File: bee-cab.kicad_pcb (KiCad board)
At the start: 2 copper layers, 29 x 53.3 mm, 34 parts, among them J1 Conn_01x02_Male, J10 Conn_01x01, J11 Conn_02x01, J12 Conn_02x01, J13 Conn_01x02, J14 Conn_01x02, J15 Conn_01x02, J16 Conn_01x02, J17 Conn_01x03, J18 Conn_01x02, J19 Conn_01x02, J2 Conn_01x02_Male, J3 Conn_01x02_Male, J4 Conn_01x02_Male, J5 Conn_01x03, J6 Conn_02x03_Odd_Even, J7 Conn_02x01, J8 Conn_01x02, J9 Conn_01x02

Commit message: Layout.
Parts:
- moved J7 2.54 mm to (85.1, 118.1), turned to 270 degrees
- moved R2 1.27 mm to (88.9, 130.8)
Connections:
- C2 pad 2: Net-(C1-Pad2) -> Net-(C1-Pad1)
- J17 pad 1: Net-(C1-Pad2) -> Net-(C1-Pad1)
- J18 pad 1: Net-(C1-Pad2) -> Net-(C1-Pad1)
- J18 pad 2: Net-(C1-Pad2) -> Net-(C1-Pad1)
- J5 pad 3: Net-(C1-Pad2) -> Net-(C1-Pad1)
- J6 pad 1: Net-(C1-Pad1) -> Net-(C1-Pad2)
- J7 pad 1: Net-(C1-Pad2) -> Net-(C1-Pad1)
- J9 pad 1: Net-(C1-Pad2) -> Net-(C1-Pad1)
- J9 pad 2: Net-(C1-Pad2) -> Net-(C1-Pad1)
- R1 pad 2: Net-(C1-Pad2) -> Net-(C1-Pad1)
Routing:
- net -15V: track 0.00 -> 97.9 mm, vias 1 -> 0
- net Net-(C1-Pad1): track 0.00 -> 76.7 mm
- net +15V: track 0.00 -> 61.8 mm
- net GND: track 0.00 -> 47.3 mm
- net Net-(J12-Pad1): track 0.00 -> 21.6 mm
- net +5V: track 0.00 -> 21.3 mm
- net Net-(C1-Pad2): track 0.00 -> 15.0 mm
- net Net-(R2-Pad1): track 0.00 -> 6.77 mm, vias 1 -> 0
- net Net-(J7-Pad2): track 0.00 -> 5.08 mm
- net Net-(J12-Pad2): track 0.00 -> 4.05 mm
- net Net-(J11-Pad2): track 0.00 -> 4.05 mm
- net Net-(J6-Pad5): track 0.00 -> 3.81 mm
- net Net-(C2-Pad1): track 0.00 -> 3.81 mm
- net (no net): vias 2 -> 4
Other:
- net class Default: trace_width 0.25 -> 0.5

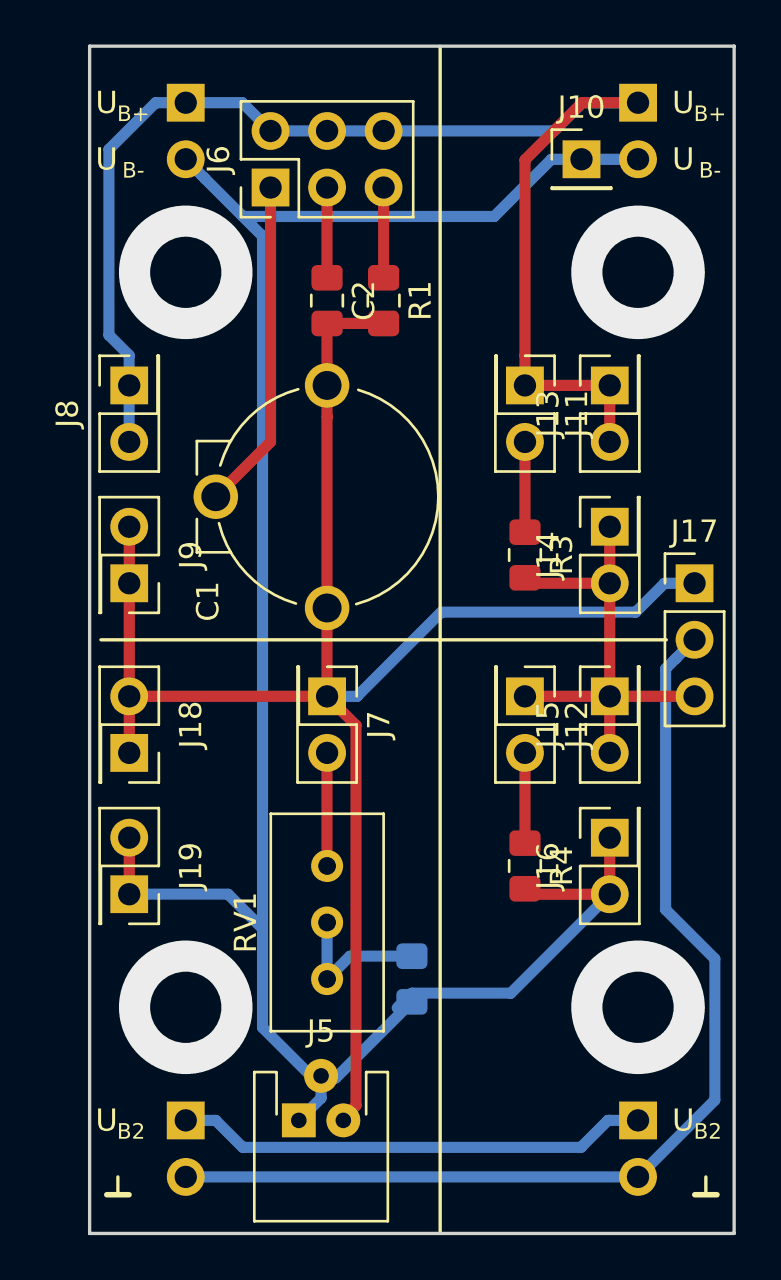
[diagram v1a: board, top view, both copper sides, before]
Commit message: Place part references on silkscreen.
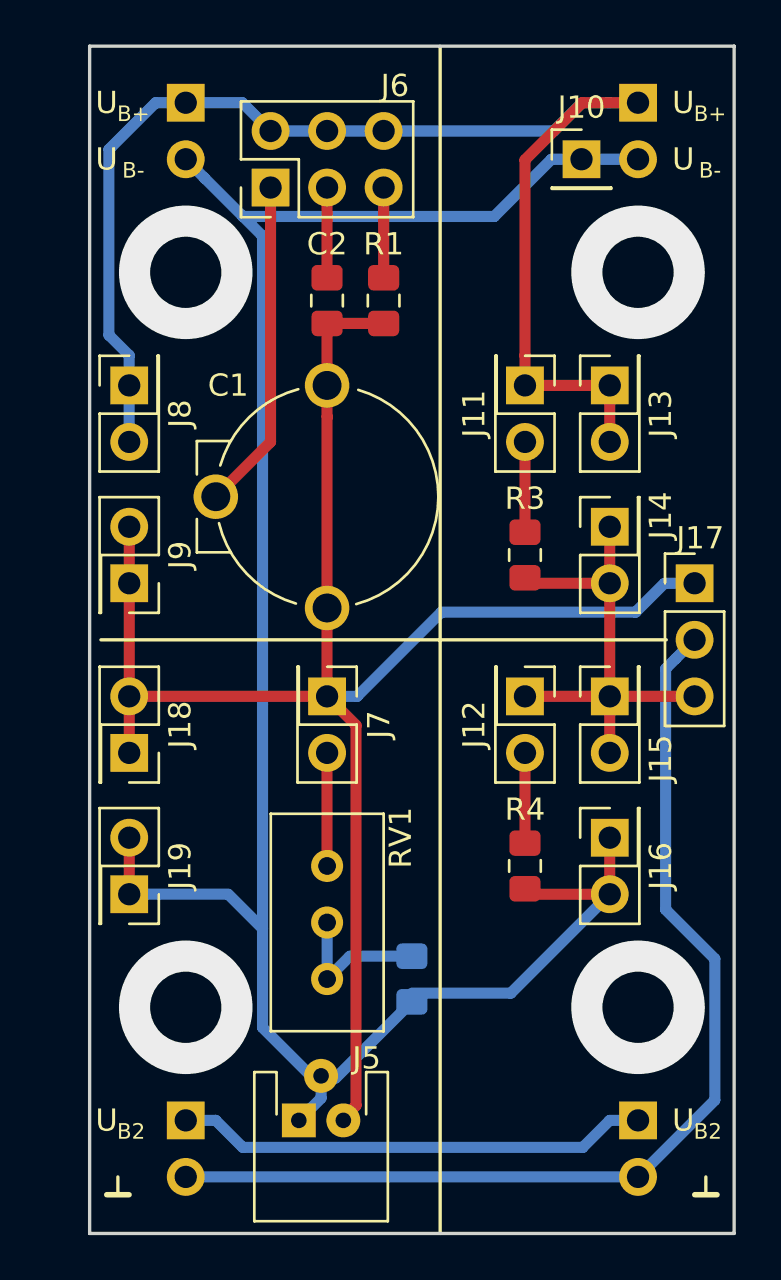
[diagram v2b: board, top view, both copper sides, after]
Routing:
- net -15V: track 97.9 -> 97.0 mm

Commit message: Add sch symbols for labels, update PCB accordingly.
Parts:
- removed REF** (x2): Text_U_B+_Silkscreen, Symbol-emt:Text_U_B+_Silkscreen
- removed REF** (x2): Text_U_B-_Silkscreen, Symbol-emt:Text_U_B-_Silkscreen
- removed REF** (x2): Text_U_B2_Silkscreen, Symbol-emt:Text_U_B2_Silkscreen
- removed REF** (x2): Symbol_GND_Silkscreen, Symbol-emt:Symbol_GND_Silkscreen
- added H1: Silkscreen_Label, Symbol-emt:Text_U_B+_Silkscreen, F.Cu at (75.2, 91.4)
- added H2: Silkscreen_Label, Symbol-emt:Text_U_B+_Silkscreen, F.Cu at (101.1, 91.4)
- added H3: Silkscreen_Label, Symbol-emt:Text_U_B-_Silkscreen, F.Cu at (75.2, 94.0)
- added H4: Silkscreen_Label, Symbol-emt:Text_U_B-_Silkscreen, F.Cu at (101.1, 94.0)
- added H5: Silkscreen_Label, Symbol-emt:Text_U_B2_Silkscreen, F.Cu at (75.2, 137.2)
- added H6: Silkscreen_Label, Symbol-emt:Text_U_B2_Silkscreen, F.Cu at (101.1, 137.2)
- added H7: Silkscreen_Label, Symbol-emt:Symbol_GND_Silkscreen, F.Cu at (75.7, 139.7)
- added H8: Silkscreen_Label, Symbol-emt:Symbol_GND_Silkscreen, F.Cu at (102.1, 139.7)

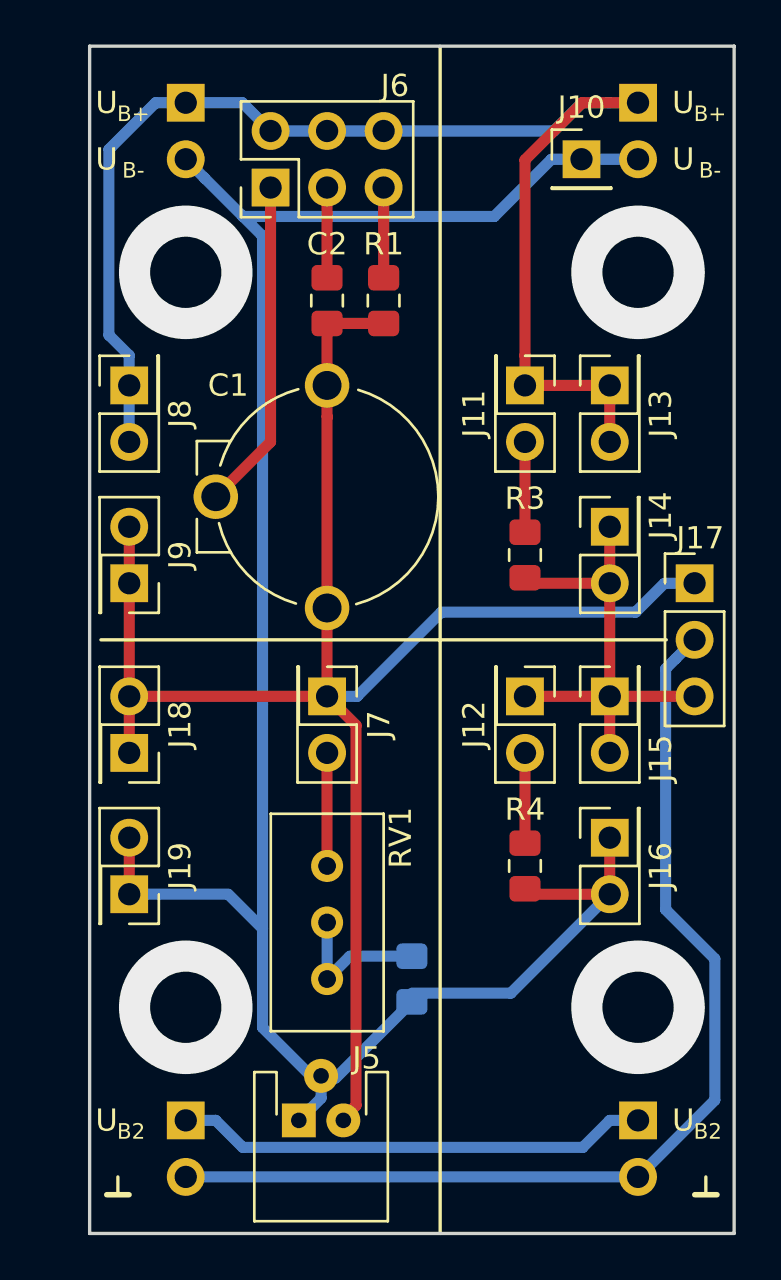
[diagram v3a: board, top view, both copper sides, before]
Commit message: Replace vias by mounting holes.
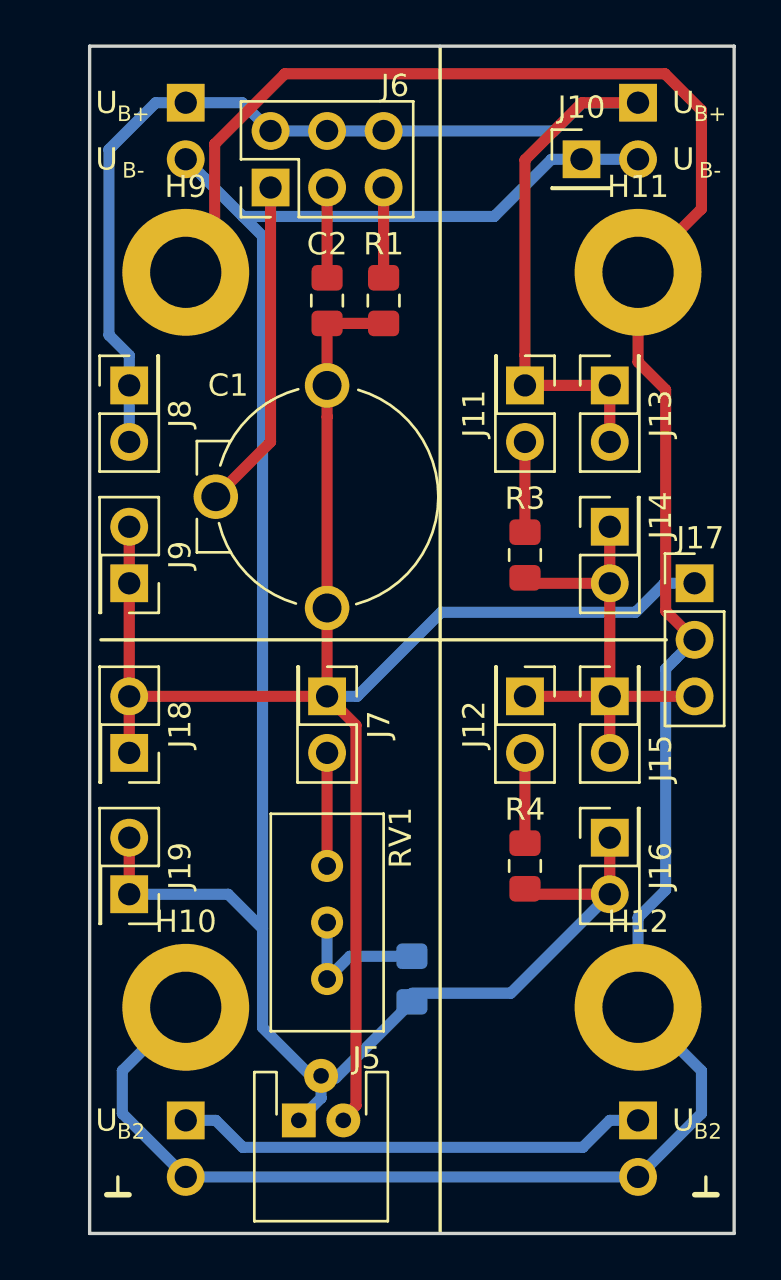
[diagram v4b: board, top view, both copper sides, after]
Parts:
- added H10: MountingHole_Pad, MountingHole:MountingHole_3.2mm_M3_ISO7380_Pad, F.Cu at (78.7, 132.1)
- added H11: MountingHole_Pad, MountingHole:MountingHole_3.2mm_M3_ISO7380_Pad, F.Cu at (99.1, 99.1)
- added H12: MountingHole_Pad, MountingHole:MountingHole_3.2mm_M3_ISO7380_Pad, F.Cu at (99.1, 132.1)
- added H9: MountingHole_Pad, MountingHole:MountingHole_3.2mm_M3_ISO7380_Pad, F.Cu at (78.7, 99.1)
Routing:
- net GND: track 47.3 -> 114.0 mm
- net (no net): vias 4 -> 0
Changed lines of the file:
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@@
     (thickness 1.6)
     (drawings 6)
-    (tracks 92)
+    (tracks 104)
     (zones 0)
-    (modules 34)
+    (modules 38)
     (nets 14)
   )
@@
     (fp_line (start 0 0.8) (end 0 0) (layer F.SilkS) (width 0.15))
   )
+  (module MountingHole:MountingHole_3.2mm_M3_ISO7380_Pad locked (layer F.Cu)
+    (at 78.74 99.06)
+    (descr "Mounting Hole 3.2mm, M3, ISO7380")
+    (tags "mounting hole 3.2mm m3 iso7380")
+    (attr virtual)
+    (fp_text reference H9 (at 0 -3.85) (layer F.SilkS)
+      (effects (font (size 1 1) (thickness 0.15)))
+    )
+    (fp_text value MountingHole_Pad (at 0 3.85) (layer F.Fab)
+      (effects (font (size 1 1) (thickness 0.15)))
+    )
+    (fp_text user %R (at 0.3 0) (layer F.Fab)
+      (effects (font (size 1 1) (thickness 0.15)))
+    )
+    (fp_circle (center 0 0) (end 2.85 0) (layer Cmts.User) (width 0.15))
+    (fp_circle (center 0 0) (end 3.1 0) (layer F.CrtYd) (width 0.05))
+    (pad 1 thru_hole circle (at 0 0) (size 5.7 5.7) (drill 3.2) (layers *.Cu *.Mask)
+      (net 3 GND))
+  )
+  (module MountingHole:MountingHole_3.2mm_M3_ISO7380_Pad locked (layer F.Cu)
+    (at 78.74 132.08)
+    (descr "Mounting Hole 3.2mm, M3, ISO7380")
+    (tags "mounting hole 3.2mm m3 iso7380")
+    (attr virtual)
+    (fp_text reference H10 (at 0 -3.85) (layer F.SilkS)
+      (effects (font (size 1 1) (thickness 0.15)))
+    )
+    (fp_text value MountingHole_Pad (at 0 3.85) (layer F.Fab)
+      (effects (font (size 1 1) (thickness 0.15)))
+    )
+    (fp_text user %R (at 0.3 0) (layer F.Fab)
+      (effects (font (size 1 1) (thickness 0.15)))
+    )
+    (fp_circle (center 0 0) (end 2.85 0) (layer Cmts.User) (width 0.15))
+    (fp_circle (center 0 0) (end 3.1 0) (layer F.CrtYd) (width 0.05))
+    (pad 1 thru_hole circle (at 0 0) (size 5.7 5.7) (drill 3.2) (layers *.Cu *.Mask)
+      (net 3 GND))
+  )
+  (module MountingHole:MountingHole_3.2mm_M3_ISO7380_Pad locked (layer F.Cu)
+    (at 99.06 99.06)
+    (descr "Mounting Hole 3.2mm, M3, ISO7380")
+    (tags "mounting hole 3.2mm m3 iso7380")
+    (attr virtual)
+    (fp_text reference H11 (at 0 -3.85) (layer F.SilkS)
+      (effects (font (size 1 1) (thickness 0.15)))
+    )
+    (fp_text value MountingHole_Pad (at 0 3.85) (layer F.Fab)
+      (effects (font (size 1 1) (thickness 0.15)))
+    )
+    (fp_circle (center 0 0) (end 3.1 0) (layer F.CrtYd) (width 0.05))
+    (fp_circle (center 0 0) (end 2.85 0) (layer Cmts.User) (width 0.15))
+    (fp_text user %R (at 0.3 0) (layer F.Fab)
+      (effects (font (size 1 1) (thickness 0.15)))
+    )
+    (pad 1 thru_hole circle (at 0 0) (size 5.7 5.7) (drill 3.2) (layers *.Cu *.Mask)
+      (net 3 GND))
+  )
+  (module MountingHole:MountingHole_3.2mm_M3_ISO7380_Pad locked (layer F.Cu)
+    (at 99.06 132.08)
+    (descr "Mounting Hole 3.2mm, M3, ISO7380")
+    (tags "mounting hole 3.2mm m3 iso7380")
+    (attr virtual)
+    (fp_text reference H12 (at 0 -3.85) (layer F.SilkS)
+      (effects (font (size 1 1) (thickness 0.15)))
+    )
+    (fp_text value MountingHole_Pad (at 0 3.85) (layer F.Fab)
+      (effects (font (size 1 1) (thickness 0.15)))
+    )
+    (fp_circle (center 0 0) (end 3.1 0) (layer F.CrtYd) (width 0.05))
+    (fp_circle (center 0 0) (end 2.85 0) (layer Cmts.User) (width 0.15))
+    (fp_text user %R (at 0.3 0) (layer F.Fab)
+      (effects (font (size 1 1) (thickness 0.15)))
+    )
+    (pad 1 thru_hole circle (at 0 0) (size 5.7 5.7) (drill 3.2) (layers *.Cu *.Mask)
+      (net 3 GND))
+  )
   (gr_line (start 74.93 115.57) (end 100.33 115.57) (layer F.SilkS) (width 0.15))
   (gr_line (start 90.17 88.9) (end 90.17 142.24) (layer F.SilkS) (width 0.15))
@@
   (gr_line (start 74.422 88.9) (end 103.378 88.9) (layer Edge.Cuts) (width 0.15))
   (gr_line (start 74.422 88.9) (end 74.422 142.24) (layer Edge.Cuts) (width 0.15))
-  (via (at 99.06 99.06) (size 6) (drill 3.2) (layers F.Cu B.Cu) (net 0) (status 40000))
-  (via (at 78.74 132.08) (size 6) (drill 3.2) (layers F.Cu B.Cu) (net 0) (status 40000))
-  (via (at 99.06 132.08) (size 6) (drill 3.2) (layers F.Cu B.Cu) (net 0) (status 40000))
-  (via (at 78.74 99.06) (size 6) (drill 3.2) (layers F.Cu B.Cu) (net 0) (status 40000))
   (segment (start 76.2 124.46) (end 76.2 127) (width 0.5) (layer F.Cu) (net 1))
   (segment (start 99.06 93.98) (end 96.52 93.98) (width 0.5) (layer B.Cu) (net 1))
@@
   (segment (start 93.98 102.79) (end 93.98 104.14) (width 0.5) (layer F.Cu) (net 2))
   (segment (start 78.74 139.7) (end 99.06 139.7) (width 0.5) (layer B.Cu) (net 3))
+  (segment (start 75.890001 136.850001) (end 75.890001 134.929999) (width 0.5) (layer B.Cu) (net 3))
+  (segment (start 78.74 139.7) (end 75.890001 136.850001) (width 0.5) (layer B.Cu) (net 3))
+  (segment (start 75.890001 134.929999) (end 78.74 132.08) (width 0.5) (layer B.Cu) (net 3))
+  (segment (start 101.909999 136.850001) (end 101.909999 134.929999) (width 0.5) (layer B.Cu) (net 3))
+  (segment (start 99.06 139.7) (end 101.909999 136.850001) (width 0.5) (layer B.Cu) (net 3))
+  (segment (start 101.909999 134.929999) (end 99.06 132.08) (width 0.5) (layer B.Cu) (net 3))
   (segment (start 100.299999 116.870001) (end 100.750001 116.419999) (width 0.5) (layer B.Cu) (net 3))
-  (segment (start 100.299999 127.689997) (end 100.299999 116.870001) (width 0.5) (layer B.Cu) (net 3))
-  (segment (start 102.510001 129.899999) (end 100.299999 127.689997) (width 0.5) (layer B.Cu) (net 3))
-  (segment (start 99.06 139.7) (end 102.510001 136.249999) (width 0.5) (layer B.Cu) (net 3))
-  (segment (start 102.510001 136.249999) (end 102.510001 129.899999) (width 0.5) (layer B.Cu) (net 3))
+  (segment (start 100.299999 126.809493) (end 100.299999 116.870001) (width 0.5) (layer B.Cu) (net 3))
+  (segment (start 99.06 132.08) (end 99.06 128.049492) (width 0.5) (layer B.Cu) (net 3))
+  (segment (start 99.06 128.049492) (end 100.299999 126.809493) (width 0.5) (layer B.Cu) (net 3))
   (segment (start 100.750001 116.419999) (end 101.6 115.57) (width 0.5) (layer B.Cu) (net 3))
+  (segment (start 100.299999 104.330507) (end 99.06 103.090508) (width 0.5) (layer F.Cu) (net 3))
+  (segment (start 101.6 115.57) (end 100.299999 114.269999) (width 0.5) (layer F.Cu) (net 3))
+  (segment (start 100.299999 114.269999) (end 100.299999 104.330507) (width 0.5) (layer F.Cu) (net 3))
+  (segment (start 99.06 103.090508) (end 99.06 99.06) (width 0.5) (layer F.Cu) (net 3))
+  (segment (start 80.040001 93.295997) (end 80.040001 97.759999) (width 0.5) (layer F.Cu) (net 3))
+  (segment (start 83.195999 90.139999) (end 80.040001 93.295997) (width 0.5) (layer F.Cu) (net 3))
+  (segment (start 100.270001 90.139999) (end 83.195999 90.139999) (width 0.5) (layer F.Cu) (net 3))
+  (segment (start 101.909999 91.779997) (end 100.270001 90.139999) (width 0.5) (layer F.Cu) (net 3))
+  (segment (start 99.06 99.06) (end 101.909999 96.210001) (width 0.5) (layer F.Cu) (net 3))
+  (segment (start 101.909999 96.210001) (end 101.909999 91.779997) (width 0.5) (layer F.Cu) (net 3))
+  (segment (start 80.040001 97.759999) (end 78.74 99.06) (width 0.5) (layer F.Cu) (net 3))
   (segment (start 78.74 137.16) (end 80.09 137.16) (width 0.5) (layer B.Cu) (net 4))
   (segment (start 97.79 137.16) (end 99.06 137.16) (width 0.5) (layer B.Cu) (net 4))

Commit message: Add ground plane.
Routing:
- added copper zone on B.Cu, net GND
- added copper zone on F.Cu, net GND
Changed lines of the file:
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@@
   (segment (start 86.115 129.785) (end 85.09 130.81) (width 0.5) (layer B.Cu) (net 12))
   (segment (start 87.63 95.25) (end 87.63 99.06) (width 0.5) (layer F.Cu) (net 13))
+  (zone (net 3) (net_name GND) (layer F.Cu) (hatch edge 0.508)
+    (connect_pads (clearance 0.508))
+    (min_thickness 0.254)
+    (fill yes (arc_segments 32) (thermal_gap 0.508) (thermal_bridge_width 0.508))
+    (polygon
+      (pts
+        (xy 74.422 88.9) (xy 103.378 88.9) (xy 103.378 142.24) (xy 74.422 142.24)
+      )
+    )
+  )
+  (zone (net 3) (net_name GND) (layer B.Cu) (hatch edge 0.508)
+    (connect_pads (clearance 0.508))
+    (min_thickness 0.254)
+    (fill yes (arc_segments 32) (thermal_gap 0.508) (thermal_bridge_width 0.508))
+    (polygon
+      (pts
+        (xy 74.422 88.9) (xy 103.378 88.9) (xy 103.378 142.24) (xy 74.422 142.24)
+      )
+    )
+  )
 )
